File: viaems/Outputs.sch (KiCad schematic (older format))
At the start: 62 parts, among them Q1 VND7NV04, Q2 VND7NV04, Q3 VND7NV04, Q4 VND7NV04, Q5 VND7NV04, Q6 VND7NV04, Q7 VND7NV04, Q8 VND7NV04, U2 TC442xA, U3 TC442xA, U4 TC442xA, U5 TC442xA, U6 TC442xA, U7 TC442xA, U8 TC442xA

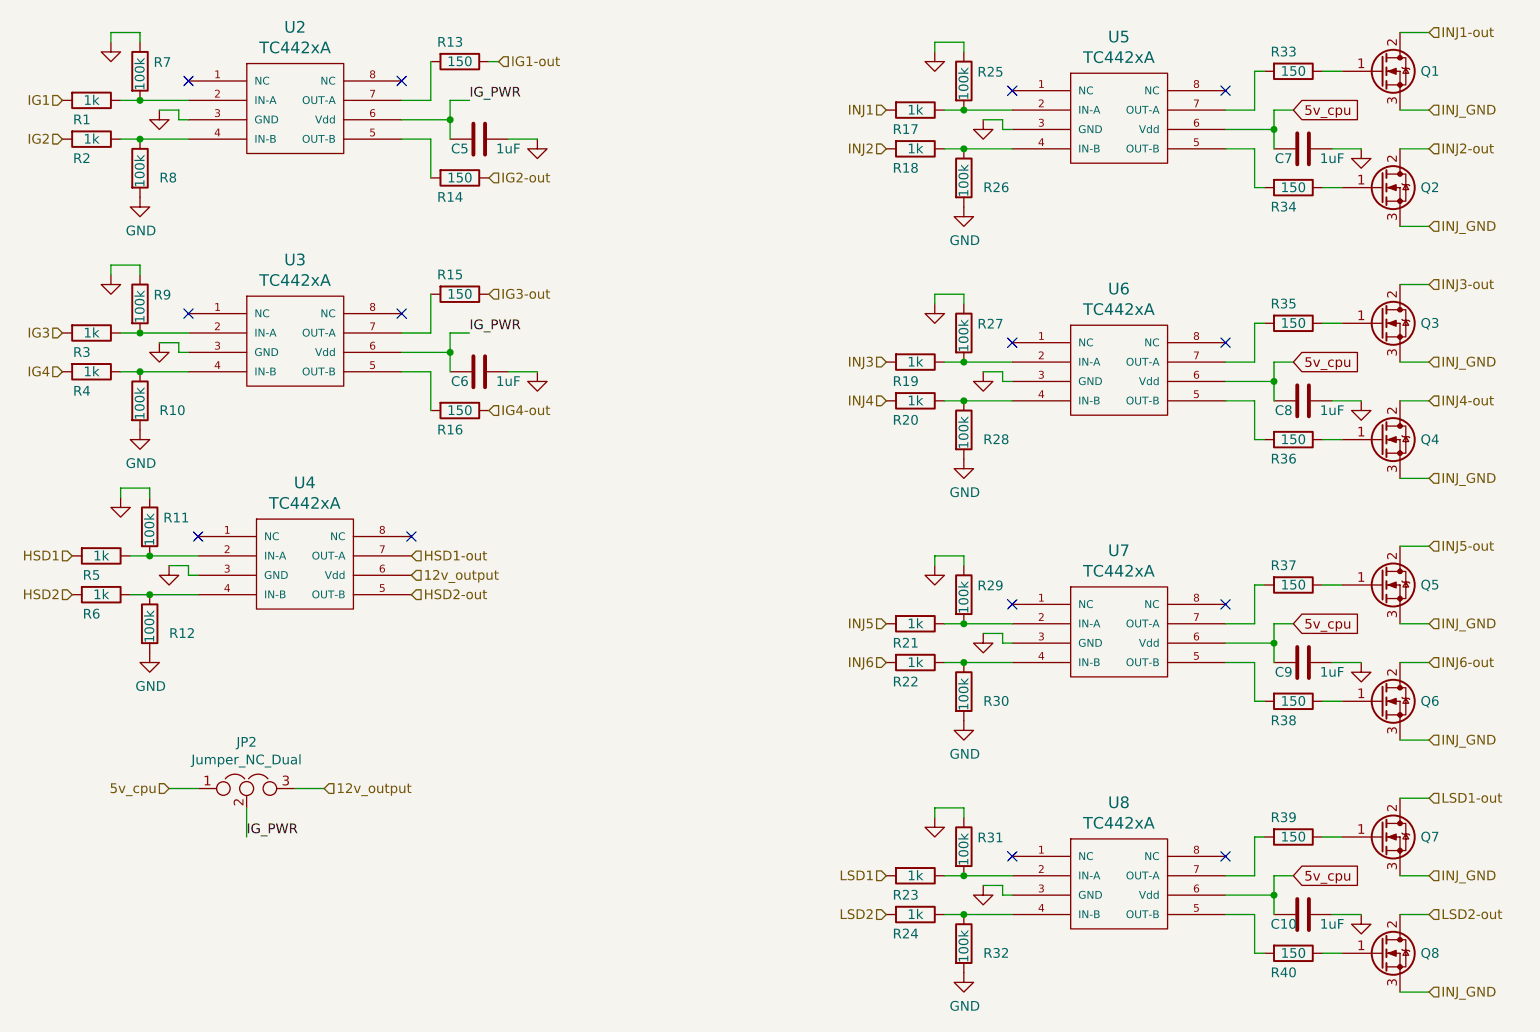
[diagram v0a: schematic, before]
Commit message: More progress. Calling schematic complete, board partially routed
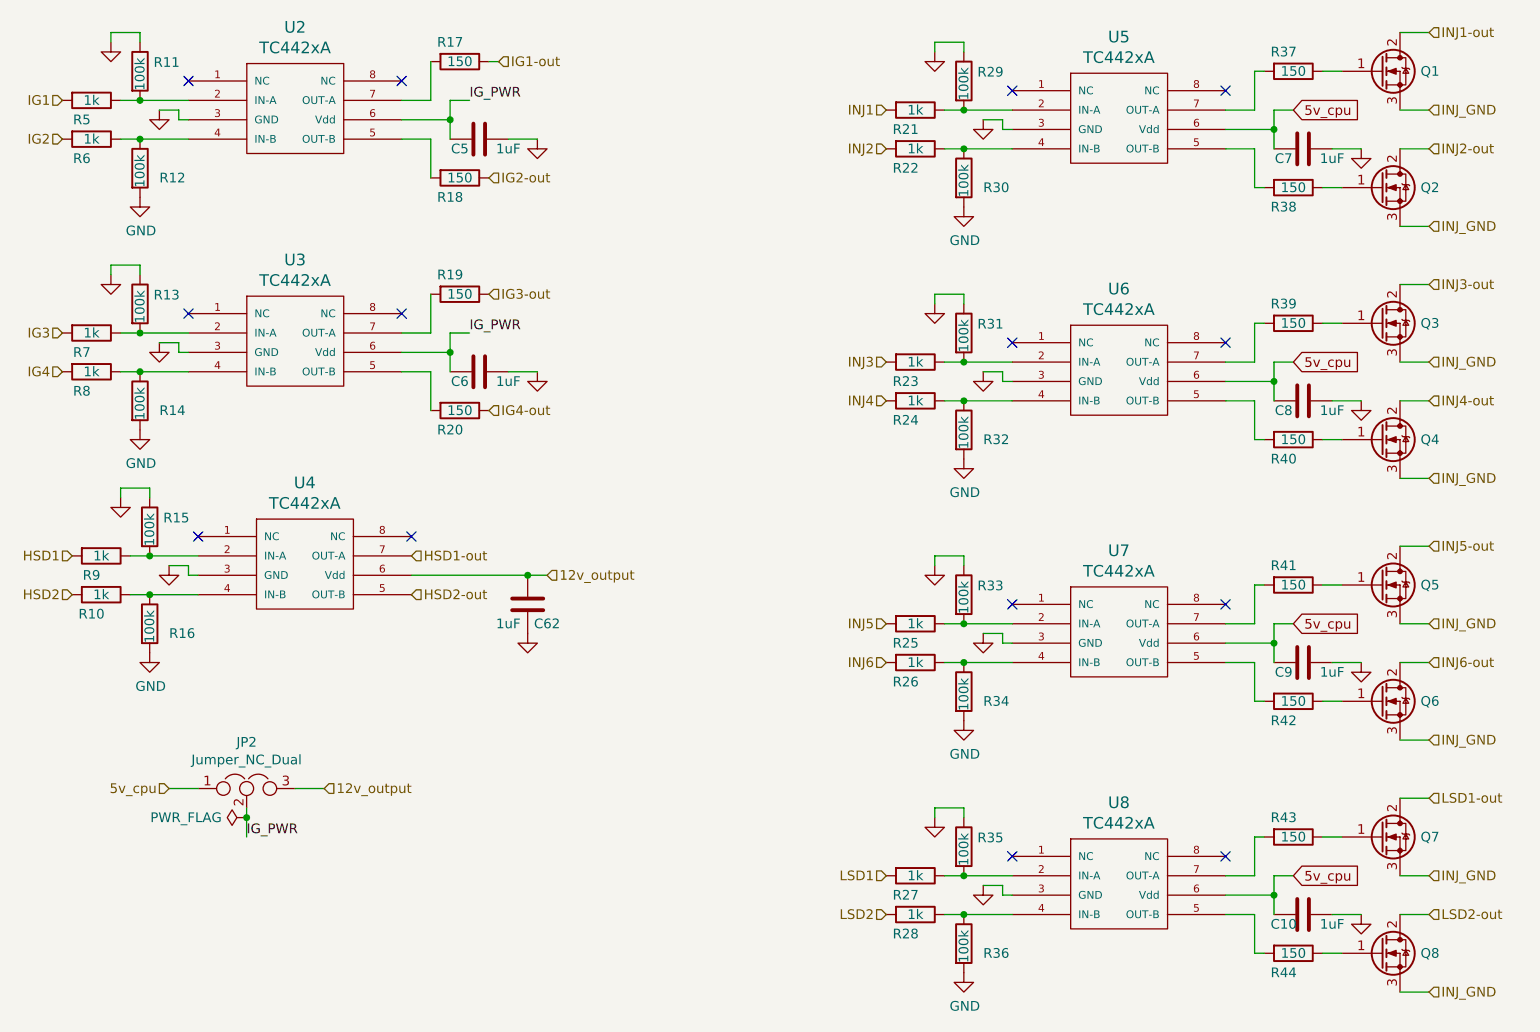
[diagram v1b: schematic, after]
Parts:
- added C62: 1uF, Capacitor_SMD:C_0805_2012Metric_Pad1.15x1.40mm_HandSolder, symbol Device:C
- C10, C7, C8, C9: footprint (none) -> Capacitor_SMD:C_0805_2012Metric_Pad1.15x1.40mm_HandSolder
- C5, C6: footprint (none) -> Capacitor_SMD:C_0805_2012Metric_Pad1.15x1.40mm_HandSolder; Digikey-Part (none) -> 1276-1029-1-ND; Notes (none) -> 35V
- JP2: footprint (none) -> Connector_PinHeader_2.54mm:PinHeader_1x03_P2.54mm_Vertical
- Q1, Q2, Q3, Q4, Q5, Q6, Q7, Q8: footprint (none) -> Package_TO_SOT_SMD:TO-252-2
- R10: renamed from R6; footprint (none) -> Resistor_SMD:R_0805_2012Metric_Pad1.15x1.40mm_HandSolder
- R11: renamed from R7; footprint (none) -> Resistor_SMD:R_0805_2012Metric_Pad1.15x1.40mm_HandSolder
- R12: renamed from R8; footprint (none) -> Resistor_SMD:R_0805_2012Metric_Pad1.15x1.40mm_HandSolder
- R13: renamed from R9; footprint (none) -> Resistor_SMD:R_0805_2012Metric_Pad1.15x1.40mm_HandSolder
- R14: renamed from R10; footprint (none) -> Resistor_SMD:R_0805_2012Metric_Pad1.15x1.40mm_HandSolder
- R15: renamed from R11; footprint (none) -> Resistor_SMD:R_0805_2012Metric_Pad1.15x1.40mm_HandSolder
- R16: renamed from R12; footprint (none) -> Resistor_SMD:R_0805_2012Metric_Pad1.15x1.40mm_HandSolder
- R17: renamed from R13; footprint (none) -> Resistor_SMD:R_2512_6332Metric_Pad1.52x3.35mm_HandSolder; Digikey-Part (none) -> 541-150XCT-ND; Notes (none) -> 1W
- R18: renamed from R14; footprint (none) -> Resistor_SMD:R_2512_6332Metric_Pad1.52x3.35mm_HandSolder; Digikey-Part (none) -> 541-150XCT-ND; Notes (none) -> 1W
- R19: renamed from R15; footprint (none) -> Resistor_SMD:R_2512_6332Metric_Pad1.52x3.35mm_HandSolder; Digikey-Part (none) -> 541-150XCT-ND; Notes (none) -> 1W
- R20: renamed from R16; footprint (none) -> Resistor_SMD:R_2512_6332Metric_Pad1.52x3.35mm_HandSolder; Digikey-Part (none) -> 541-150XCT-ND; Notes (none) -> 1W
- R21: renamed from R17; footprint (none) -> Resistor_SMD:R_0805_2012Metric_Pad1.15x1.40mm_HandSolder
- R22: renamed from R18; footprint (none) -> Resistor_SMD:R_0805_2012Metric_Pad1.15x1.40mm_HandSolder
- R23: renamed from R19; footprint (none) -> Resistor_SMD:R_0805_2012Metric_Pad1.15x1.40mm_HandSolder
- R24: renamed from R20; footprint (none) -> Resistor_SMD:R_0805_2012Metric_Pad1.15x1.40mm_HandSolder
- R25: renamed from R21; footprint (none) -> Resistor_SMD:R_0805_2012Metric_Pad1.15x1.40mm_HandSolder
- R26: renamed from R22; footprint (none) -> Resistor_SMD:R_0805_2012Metric_Pad1.15x1.40mm_HandSolder
- R27: renamed from R23; footprint (none) -> Resistor_SMD:R_0805_2012Metric_Pad1.15x1.40mm_HandSolder
- R28: renamed from R24; footprint (none) -> Resistor_SMD:R_0805_2012Metric_Pad1.15x1.40mm_HandSolder
- R29: renamed from R25; footprint (none) -> Resistor_SMD:R_0805_2012Metric_Pad1.15x1.40mm_HandSolder
- R30: renamed from R26; footprint (none) -> Resistor_SMD:R_0805_2012Metric_Pad1.15x1.40mm_HandSolder
- R31: renamed from R27; footprint (none) -> Resistor_SMD:R_0805_2012Metric_Pad1.15x1.40mm_HandSolder
- R32: renamed from R28; footprint (none) -> Resistor_SMD:R_0805_2012Metric_Pad1.15x1.40mm_HandSolder
- R33: renamed from R29; footprint (none) -> Resistor_SMD:R_0805_2012Metric_Pad1.15x1.40mm_HandSolder
- R34: renamed from R30; footprint (none) -> Resistor_SMD:R_0805_2012Metric_Pad1.15x1.40mm_HandSolder
- R35: renamed from R31; footprint (none) -> Resistor_SMD:R_0805_2012Metric_Pad1.15x1.40mm_HandSolder
- R36: renamed from R32; footprint (none) -> Resistor_SMD:R_0805_2012Metric_Pad1.15x1.40mm_HandSolder
- R37: renamed from R33; footprint (none) -> Resistor_SMD:R_0805_2012Metric_Pad1.15x1.40mm_HandSolder
- R38: renamed from R34; footprint (none) -> Resistor_SMD:R_0805_2012Metric_Pad1.15x1.40mm_HandSolder
- R39: renamed from R35; footprint (none) -> Resistor_SMD:R_0805_2012Metric_Pad1.15x1.40mm_HandSolder
- R40: renamed from R36; footprint (none) -> Resistor_SMD:R_0805_2012Metric_Pad1.15x1.40mm_HandSolder
- R41: renamed from R37; footprint (none) -> Resistor_SMD:R_0805_2012Metric_Pad1.15x1.40mm_HandSolder
- R42: renamed from R38; footprint (none) -> Resistor_SMD:R_0805_2012Metric_Pad1.15x1.40mm_HandSolder
- R43: renamed from R39; footprint (none) -> Resistor_SMD:R_0805_2012Metric_Pad1.15x1.40mm_HandSolder
- R44: renamed from R40; footprint (none) -> Resistor_SMD:R_0805_2012Metric_Pad1.15x1.40mm_HandSolder
- R5: renamed from R1; footprint (none) -> Resistor_SMD:R_0805_2012Metric_Pad1.15x1.40mm_HandSolder
- R6: renamed from R2; footprint (none) -> Resistor_SMD:R_0805_2012Metric_Pad1.15x1.40mm_HandSolder
- R7: renamed from R3; footprint (none) -> Resistor_SMD:R_0805_2012Metric_Pad1.15x1.40mm_HandSolder
- R8: renamed from R4; footprint (none) -> Resistor_SMD:R_0805_2012Metric_Pad1.15x1.40mm_HandSolder
- R9: renamed from R5; footprint (none) -> Resistor_SMD:R_0805_2012Metric_Pad1.15x1.40mm_HandSolder
- U2, U3, U4, U5, U6, U7, U8: footprint (none) -> Package_SO:SOIC-8_3.9x4.9mm_P1.27mm; Digikey-Part (none) -> TC4427EOA713CT-ND
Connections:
- net 12v_output: now also C62.2
- net GND: now also C62.1

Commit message: Misc fixes
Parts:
- C10, C7, C8, C9: Digikey-Part (none) -> 1276-1029-1-ND
- JP2: Digikey-Part (none) -> 732-5316-ND
- Q1, Q2, Q3, Q4, Q5, Q6, Q7, Q8: Digikey-Part (none) -> 497-11707-1-ND
- R10, R21, R22, R23, R24, R25, R26, R27, R28, R5, R6, R7, R8, R9: Digikey-Part (none) -> RNCP0805FTD1K00CT-ND
- R11, R12, R13, R14, R15, R16, R29, R30, R31, R32, R33, R34, R35, R36: Digikey-Part (none) -> P100KDACT-ND
- R37, R38, R39, R40, R41, R42, R43, R44: Digikey-Part (none) -> RNCP0805FTD150RCT-ND
